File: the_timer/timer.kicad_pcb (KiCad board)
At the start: 2 copper layers, 18 x 37.5 mm, 20 parts, among them J1 AVR-ISP-6, J2 Conn_01x04_Socket, J3 Conn_01x02_Socket, Q1 2N7002, Q2 2N7002, Q3 2N7002, U1 ATtiny48-A, U2 TPS61033, U3 MC3416, U4 W25Q128JVS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

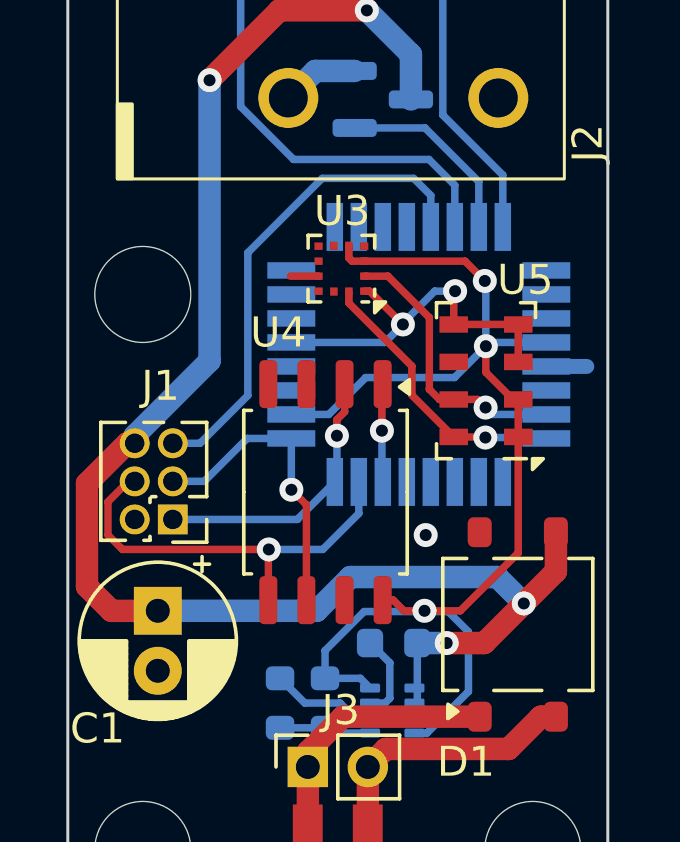
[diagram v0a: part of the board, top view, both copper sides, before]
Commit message: Added decoupling cap to barometer and rotated IMU 45 deg
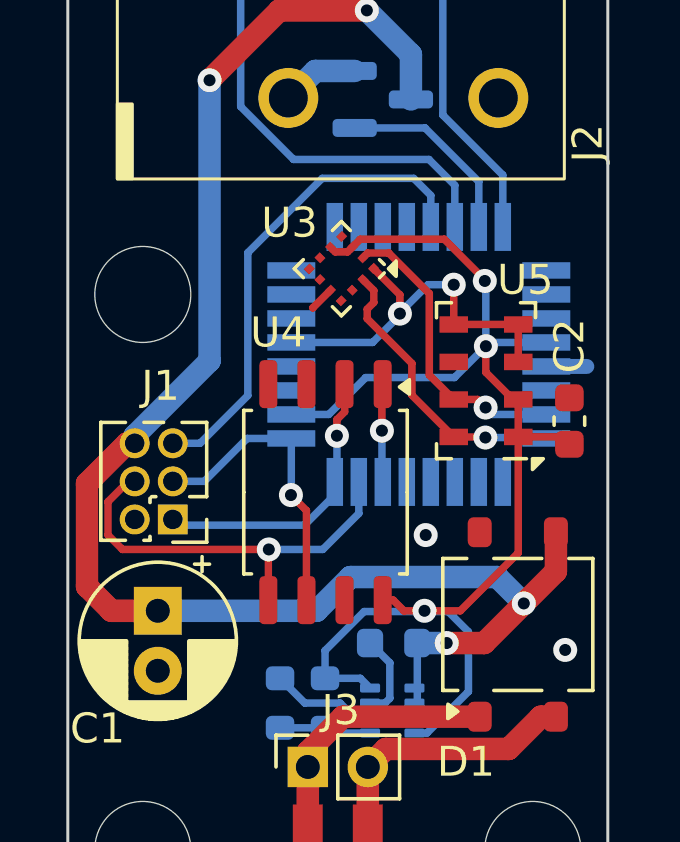
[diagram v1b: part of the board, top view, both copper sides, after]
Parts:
- added C2: 100n, Capacitor_SMD:C_0603_1608Metric, F.Cu at (222.7, 92.0)
- turned U3 to -135 degrees
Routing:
- net V_{reg}: track 42.3 -> 44.8 mm
- net SDA: track 9.38 -> 10.00 mm
- net GND: track 18.3 -> 18.6 mm, vias 3 -> 4

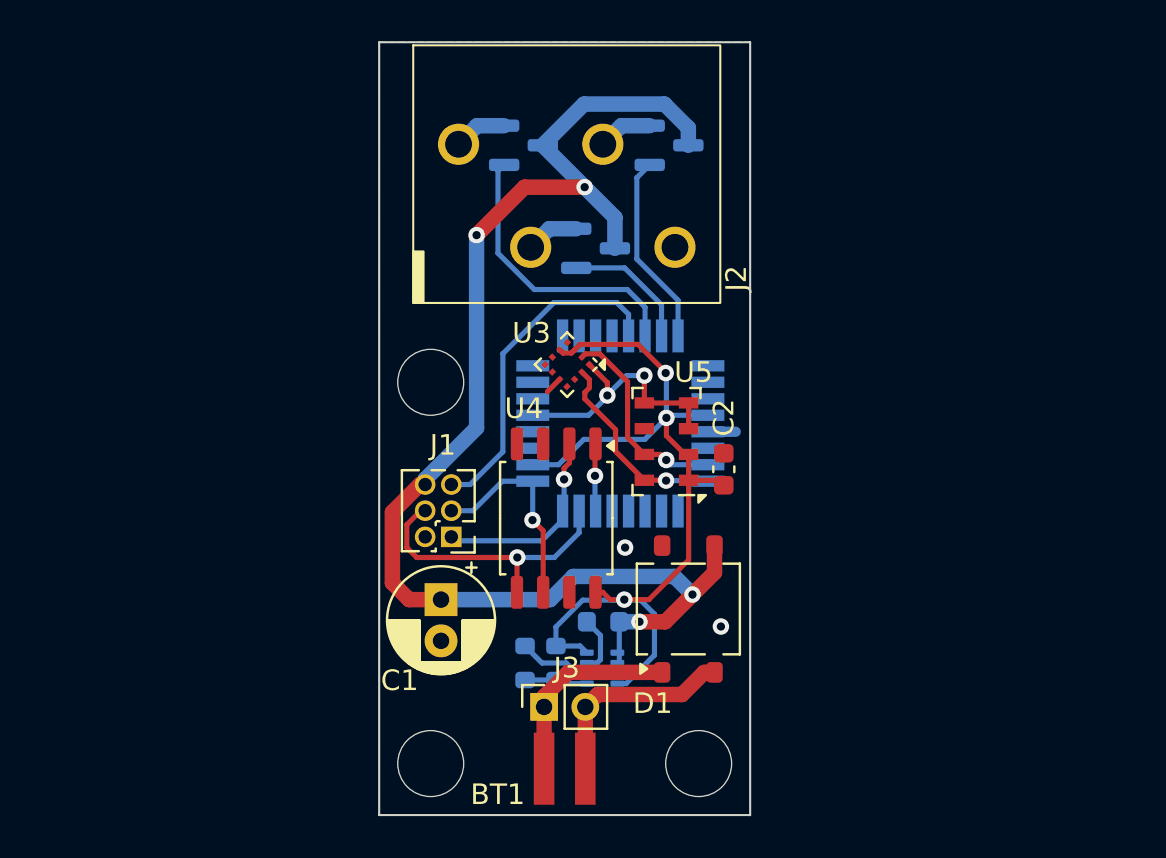
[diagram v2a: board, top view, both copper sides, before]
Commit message: Standardized names on Timer schematic
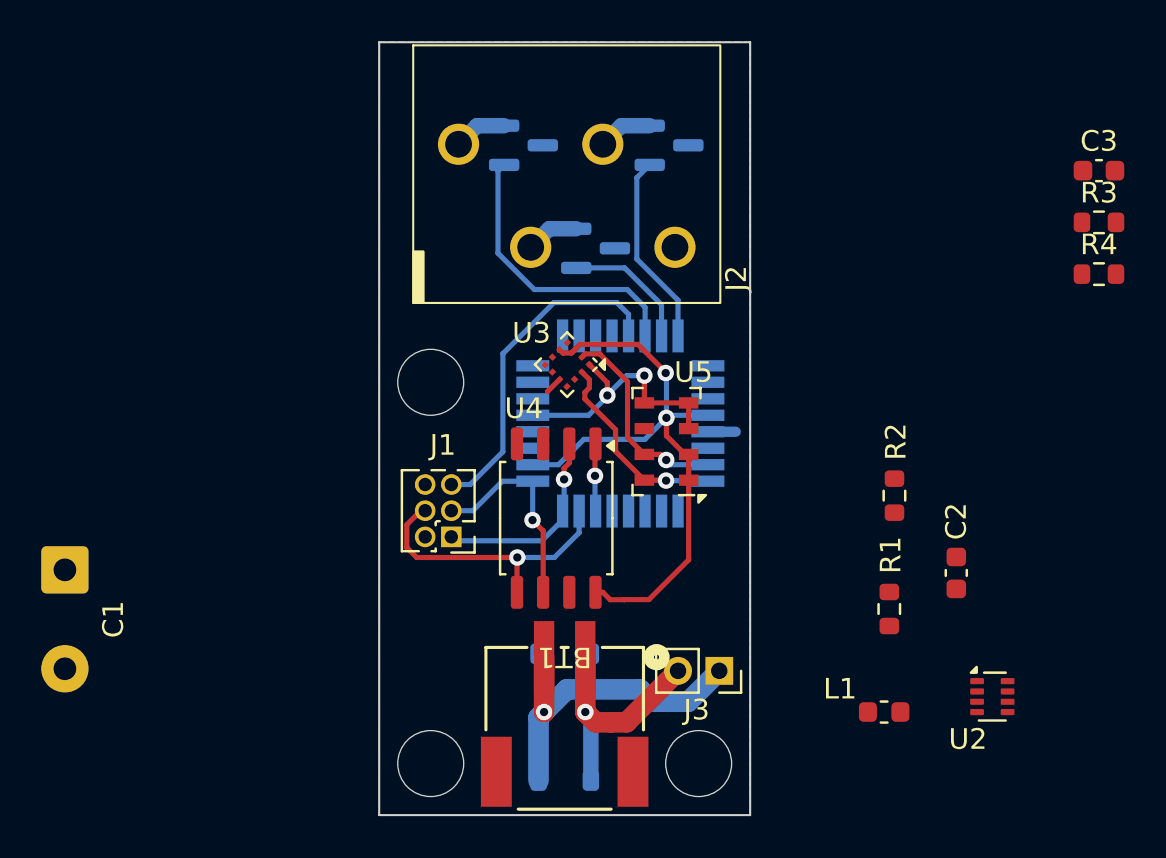
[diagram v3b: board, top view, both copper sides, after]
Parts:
- added C3: 1u, Capacitor_SMD:C_0603_1608Metric, F.Cu at (240.9, 77.5)
- added R3: 4.7k, Resistor_SMD:R_0603_1608Metric, F.Cu at (240.9, 80.0)
- added R4: 4.7k, Resistor_SMD:R_0603_1608Metric, F.Cu at (240.9, 82.5)
- BT1: value External -> Battery Cell; footprint locals:TE Right Angle JST -> locals_but_working_PLEASE:CONN2_1775469-2_TEC
- C1: value 220u -> User Provided; footprint Capacitor_THT:CP_Radial_D5.0mm_P2.00mm -> Connector_Wire:SolderWire-0.5sqmm_1x02_P4.8mm_D0.9mm_OD2.3mm
- D1: moved to B.Cu
- L1, R1, R2, U2: moved to F.Cu
- moved R2 19.7 mm to (231.0, 93.2)
- moved U2 19.0 mm to (235.8, 103.0), turned to 0 degrees
- moved C1 18.3 mm to (190.8, 96.8)
- moved R1 16.4 mm to (230.8, 98.8)
- moved L1 14.3 mm to (230.5, 103.8), turned to 180 degrees
- moved C2 12.4 mm to (234.0, 97.0)
- moved J3 8.68 mm to (222.5, 101.8), turned to -90 degrees
- moved D1 7.97 mm to (215.0, 104.0)
- moved BT1 5.77 mm to (214.0, 101.1)
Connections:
- BT1 pad 1: VB+ -> Net-(BT1-+)
- BT1 pad 2: VB- -> Net-(BT1--)
- C1 pad 1: V_{cc} -> V_{B}
- C2 pad 1: V_{reg} -> V_{CC}
- D1 pad 1: VB- -> Net-(BT1-+)
- D1 pad 2: VB+ -> Net-(BT1--)
- D1 pad 3: V_{cc} -> V_{B}
- J1 pad 2: GND -> V_{CC}
- J1 pad 6: V_{cc} -> GND
- J3 pad 1: VB- -> Net-(BT1--)
- J3 pad 2: VB+ -> Net-(BT1-+)
- L1 pad 2: V_{cc} -> V_{B}
- Q1 pad 3: V_{cc} -> V_{B}
- Q2 pad 3: V_{cc} -> V_{B}
- Q3 pad 3: V_{cc} -> V_{B}
- R1 pad 1: V_{reg} -> V_{CC}
- U1 pad 18: V_{reg} -> V_{CC}
- U1 pad 4: V_{reg} -> V_{CC}
- U2 pad 1: V_{cc} -> V_{B}
- U2 pad 2: V_{cc} -> V_{B}
- U2 pad 3: V_{cc} -> V_{B}
- U2 pad 4: V_{reg} -> V_{CC}
- U2 pad 8: V_{reg} -> V_{CC}
- U3 pad 3: V_{reg} -> V_{CC}
- U3 pad 5: V_{reg} -> V_{CC}
- U4 pad 8: V_{reg} -> V_{CC}
- U5 pad 1: V_{reg} -> V_{CC}
- U5 pad 2: V_{reg} -> V_{CC}
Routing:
- net V_{cc}: track 65.6 -> 0.00 mm, vias 4 -> 0
- net V_{reg}: track 44.8 -> 0.00 mm, vias 3 -> 0
- net V_{CC}: track 0.00 -> 30.5 mm, vias 0 -> 2
- net Net-(BT1--): track 0.00 -> 15.9 mm, vias 0 -> 1
- net Net-(BT1-+): track 0.00 -> 11.8 mm, vias 0 -> 1
- net VB+: track 9.71 -> 0.00 mm
- net VB-: track 9.47 -> 0.00 mm
- net GND: track 18.6 -> 15.0 mm, vias 4 -> 2
- net Net-(U2-SW): track 2.84 -> 0.00 mm
- net Net-(U2-FB): track 2.82 -> 0.00 mm

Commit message: Updated timer PCB
this might just be the worst board ever made
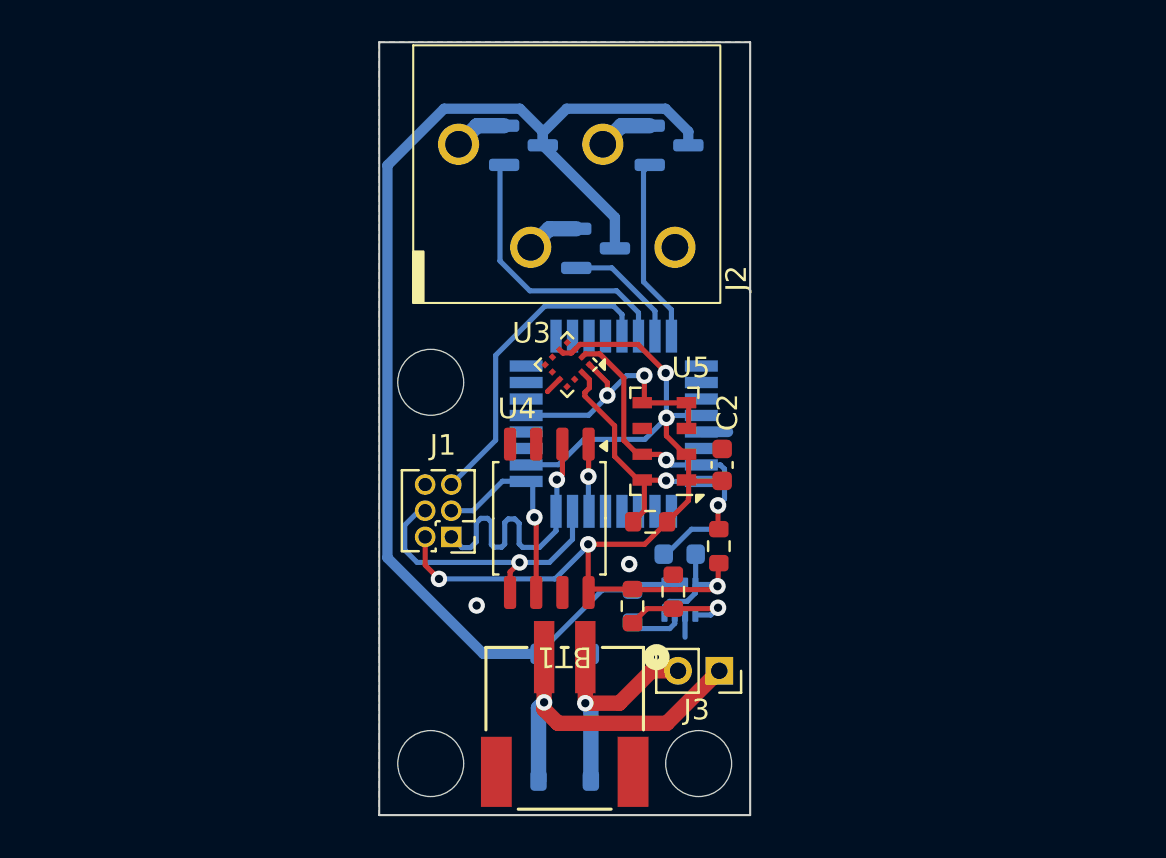
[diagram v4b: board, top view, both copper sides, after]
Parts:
- removed C1: User Provided, Connector_Wire:SolderWire-0.5sqmm_1x02_P4.8mm_D0.9mm_OD2.3mm
- C3: value 1u -> 10u; moved to B.Cu
- L1, U2: moved to B.Cu
- moved C3 27.6 mm to (220.6, 96.1), turned to 180 degrees
- moved R4 24.9 mm to (219.2, 94.5), turned to 180 degrees
- moved R3 24.2 mm to (222.5, 95.7), turned to -90 degrees
- moved U2 15.9 mm to (220.6, 98.3), turned to -90 degrees
- moved L1 13.2 mm to (218.3, 98.6), turned to 90 degrees
- moved C2 12.5 mm to (222.6, 91.8)
- moved R1 12.5 mm to (218.3, 98.6)
- moved R2 11.7 mm to (220.3, 97.9)
- moved U4 0.34 mm to (214.3, 94.3)
- moved U1 0.32 mm to (217.4, 89.8)
- moved U5 0.11 mm to (219.8, 90.6)
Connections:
- C3 pad 1: V_{B} -> V_{CC}
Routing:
- net V_{B}: track 0.00 -> 62.3 mm
- net V_{CC}: track 30.5 -> 55.0 mm, vias 2 -> 5
- net Net-(U2-FB): track 0.00 -> 5.70 mm, vias 0 -> 1
- net MISO: track 9.73 -> 15.0 mm
- net GND: track 15.0 -> 19.6 mm, vias 2 -> 4
- net SDA: track 10.00 -> 14.1 mm, vias 1 -> 2
- net Net-(U2-SW): track 0.00 -> 2.69 mm
- net SCL: track 9.83 -> 11.9 mm
- net ~{RESET}: track 16.3 -> 15.5 mm
- net Net-(BT1-+): track 11.8 -> 11.3 mm

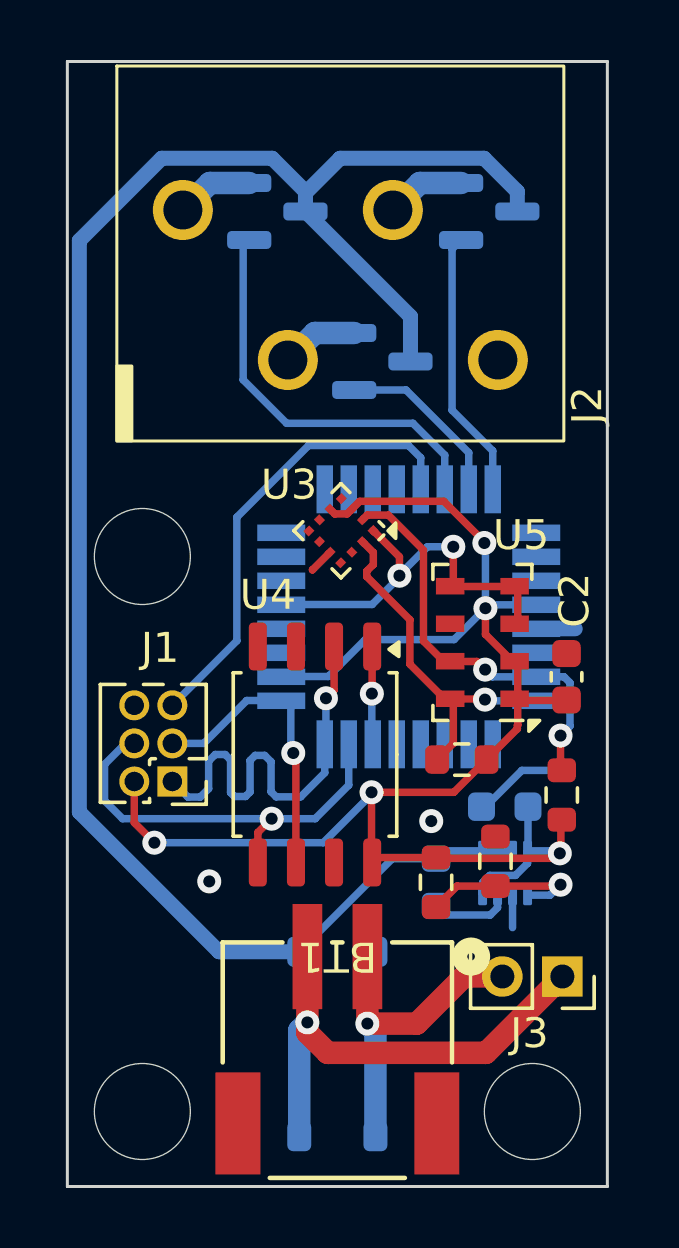
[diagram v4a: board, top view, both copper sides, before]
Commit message: Progress on altimeter implementation
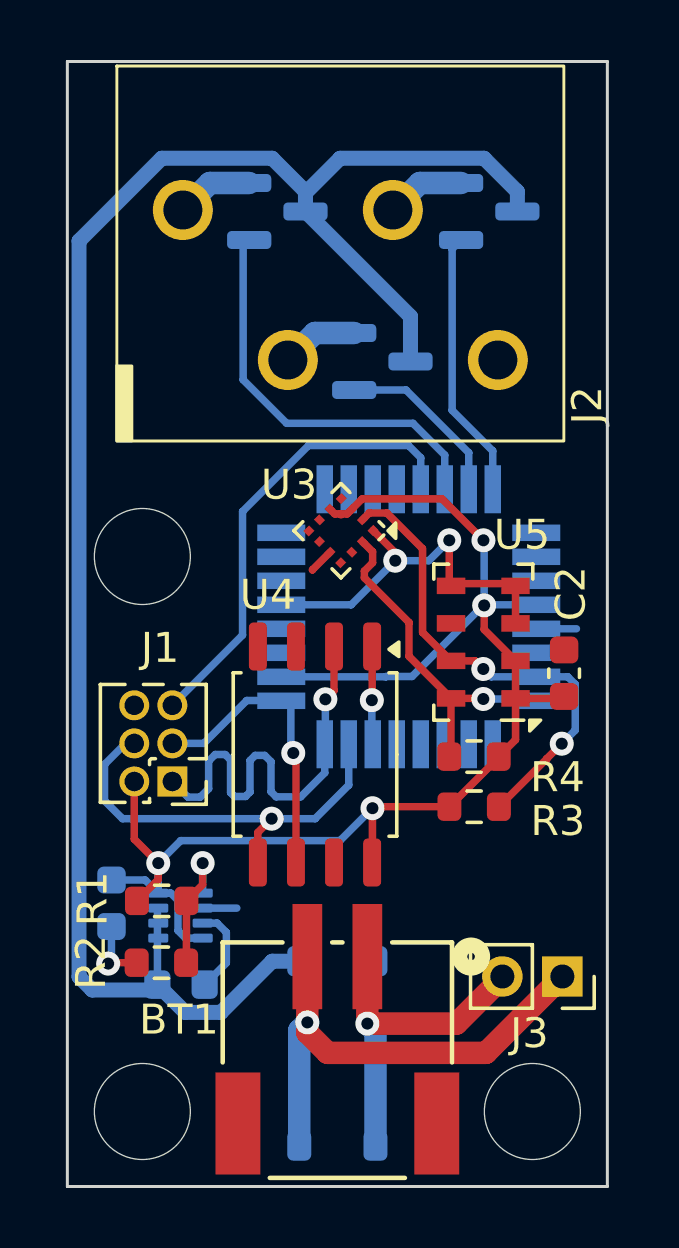
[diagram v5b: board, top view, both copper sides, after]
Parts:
- R3, R4: value 4.7k -> 10k
- moved C3 13.5 mm to (207.5, 99.3), turned to -90 degrees
- moved R2 11.6 mm to (209.1, 101.3), turned to 180 degrees
- moved U2 10.9 mm to (209.8, 99.7), turned to 0 degrees
- moved R1 9.17 mm to (209.1, 99.2), turned to 0 degrees
- moved L1 9.16 mm to (209.8, 102.0), turned to 180 degrees
- moved R3 2.95 mm to (219.6, 96.1), turned to 0 degrees
- moved R4 0.42 mm to (219.6, 94.4)
- moved D1 0.31 mm to (215.0, 104.3)
- moved C2 0.14 mm to (222.6, 91.6)
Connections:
- R3 pad 1: SDA -> V_{CC}
- R3 pad 2: V_{CC} -> SDA
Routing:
- net V_{CC}: track 55.0 -> 49.7 mm, vias 5 -> 4
- net SDA: track 14.1 -> 16.3 mm
- net GND: track 19.6 -> 18.4 mm, vias 4 -> 3
- net Net-(U2-FB): track 5.70 -> 4.55 mm
- net V_{B}: track 62.3 -> 61.3 mm

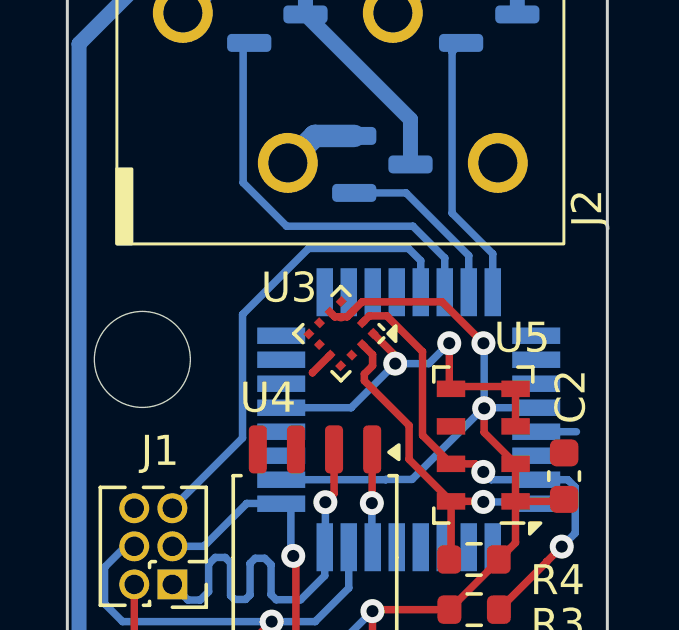
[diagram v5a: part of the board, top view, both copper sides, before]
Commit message: Added datasheets to Timer schematic
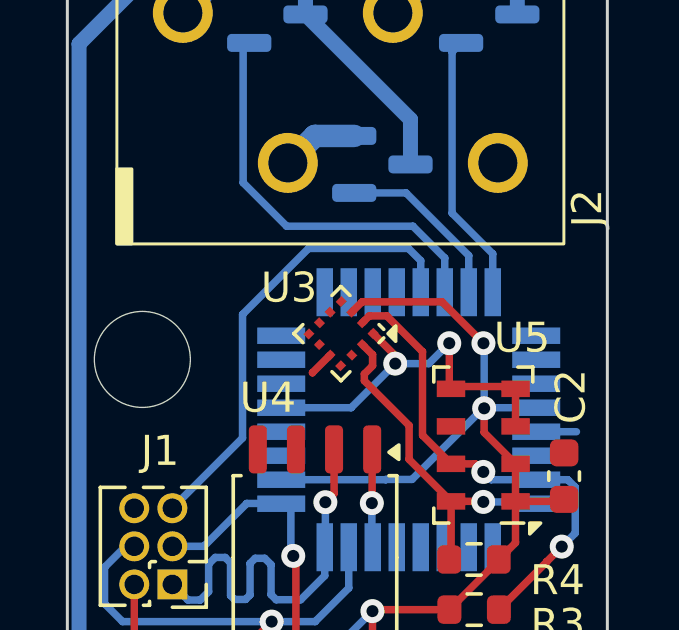
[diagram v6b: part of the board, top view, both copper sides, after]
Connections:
- U3 pad 5: V_{CC} -> unconnected-(U3-INTN-Pad5)
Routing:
- net V_{CC}: track 49.7 -> 48.8 mm
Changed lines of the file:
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@@
 	(net 46 "V_{B}")
 	(net 47 "V_{CC}")
+	(net 48 "unconnected-(U3-INTN-Pad5)")
 	(footprint "MountingHole:MountingHole_3.2mm_M3"
 		(layer "F.Cu")
@@
 		(tags "capacitor")
 		(property "Reference" "C2"
-			(at 2.65 0.22 270)
+			(at 2.65 0.22 -90)
 			(layer "F.SilkS")
 			(effects
@@
 		)
 		(property "Value" "100n"
-			(at 0 1.43 270)
+			(at 0 1.43 -90)
 			(layer "F.Fab")
 			(effects
@@
 		)
 		(fp_text user "${REFERENCE}"
-			(at 0 0 270)
+			(at 0 0 -90)
 			(layer "F.Fab")
 			(effects
@@
 			)
 		)
-		(property "Datasheet" ""
+		(property "Datasheet" "https://www.memsic.com/Public/Uploads/uploadfile/files/20220522/MC3416Datasheet(APS-045-0020v2.2).pdf"
 			(at 0 0 -135)
 			(unlocked yes)
@@
 			(size 0.25 0.275)
 			(layers "F.Cu" "F.Paste" "F.Mask")
-			(net 47 "V_{CC}")
+			(net 48 "unconnected-(U3-INTN-Pad5)")
 			(pinfunction "INTN")
 			(pintype "input")
@@
 		(tags "resistor")
 		(property "Reference" "R3"
-			(at 2.79 0.48 360)
+			(at 2.79 0.48 0)
 			(layer "F.SilkS")
 			(effects
@@
 		)
 		(property "Value" "10k"
-			(at 0 1.43 360)
+			(at 0 1.43 0)
 			(layer "F.Fab")
 			(effects
@@
 		)
 		(fp_text user "${REFERENCE}"
-			(at 0 0 360)
+			(at 0 0 0)
 			(layer "F.Fab")
 			(effects
@@
 	)
 	(segment
-		(start 215.09 86.331117)
-		(end 214.914671 86.331117)
-		(width 0.25)
-		(layer "F.Cu")
-		(net 47)
-	)
-	(segment
 		(start 218.49 85.83)
 		(end 215.826446 85.83)
@@
 	)
 	(segment
-		(start 215.482392 86.174054)
-		(end 215.325329 86.331117)
-		(width 0.25)
-		(layer "F.Cu")
-		(net 47)
-	)
-	(segment
-		(start 214.914671 86.331117)
-		(end 214.757608 86.174054)
-		(width 0.25)
-		(layer "F.Cu")
-		(net 47)
-	)
-	(segment
 		(start 209.03 97.97)
 		(end 208.23 97.17)
@@
 	)
 	(segment
-		(start 215.123262 86.364379)
-		(end 215.09 86.331117)
-		(width 0.25)
-		(layer "F.Cu")
-		(net 47)
-	)
-	(segment
 		(start 220.94 92.48)
 		(end 220.94 93.86)
@@
 		(width 0.25)
 		(layer "F.Cu")
-		(net 47)
-	)
-	(segment
-		(start 215.325329 86.331117)
-		(end 215.09 86.331117)
-		(width 0.25)
-		(layer "F.Cu")
